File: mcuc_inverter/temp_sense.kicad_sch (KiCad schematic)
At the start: 0 parts

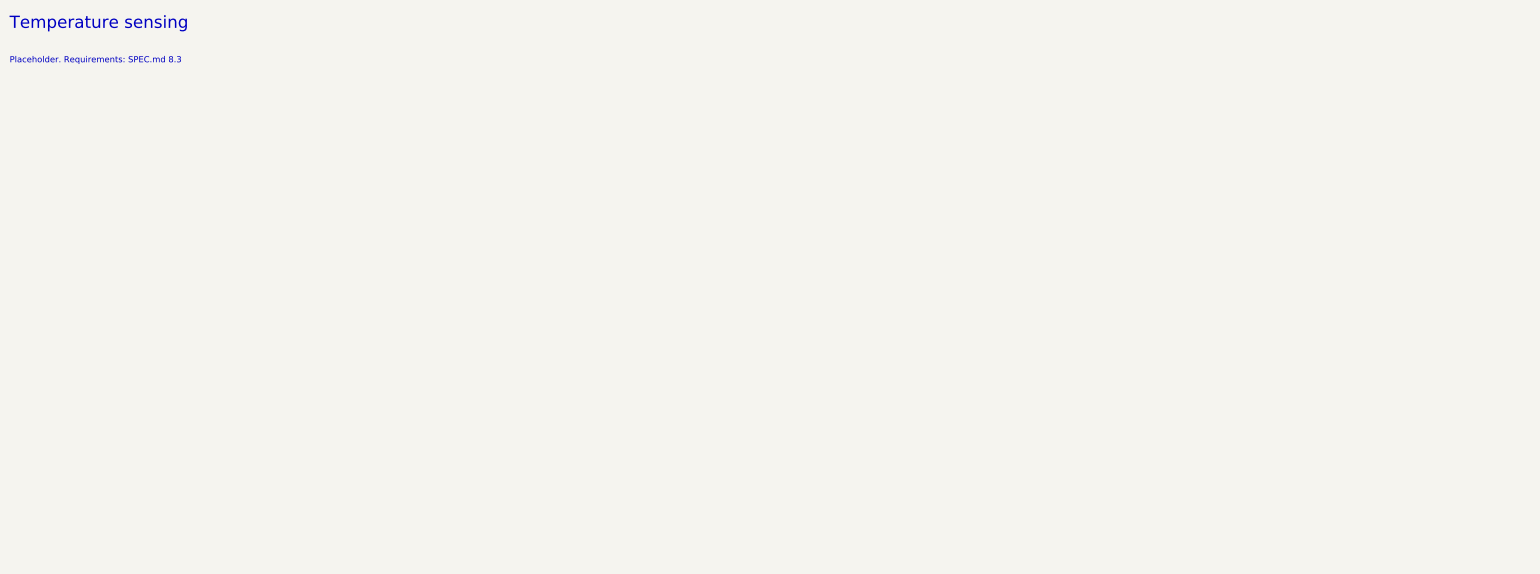
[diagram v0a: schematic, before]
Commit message: Capture bus_sense, temp_sense, comms: all 11 sheets now live
bus_sense: 4x750k + 12.0k string (strict series, 124.5 V/part) into
AMC1311BDWV (pinout verified vs SBAS786C; B-grade 3.0-5.5 V VDD1 is
load-bearing per D022; no input clamp diodes per TI 9.3), HV-side
3.3 V from MCP1804T-3302 (2-28 V in, stocked - no TBV needed) off
the VGD_LS rail, diff-to-SE gain 0.75: V_BUS = 2.988 mV/V, 500 V ->
1.494 V, saturates ~1.50 V, always < 3.3 V.

temp_sense: coldplate NTC channel (B57861S off-board via J1101),
board NTC (NCU18 successor), 6x DNP TS provision pads onto the
module TS pins with D022 rationale quoted on-sheet.

comms: ISO1042DWR isolated CAN (VCC2 pins 11/16 tied - datasheet
requirement), split termination + TVS added (legacy sheet flagged
its own missing protection), USB-C + USBLC6 to MCU 70/71, keyed SWD,
status LEDs, I/O connectors. CAN_TX/RX verified onto MCU pins 96/95;
CONTACTOR_P/N resolve onto the precharge coil driver.

ERC 0 errors; netlist machine-checks per sheet; key cross-sheet
nets independently re-verified. 11 of 11 sheets captured.

Co-Authored-By: Claude Fable 5 <noreply@anthropic.com>
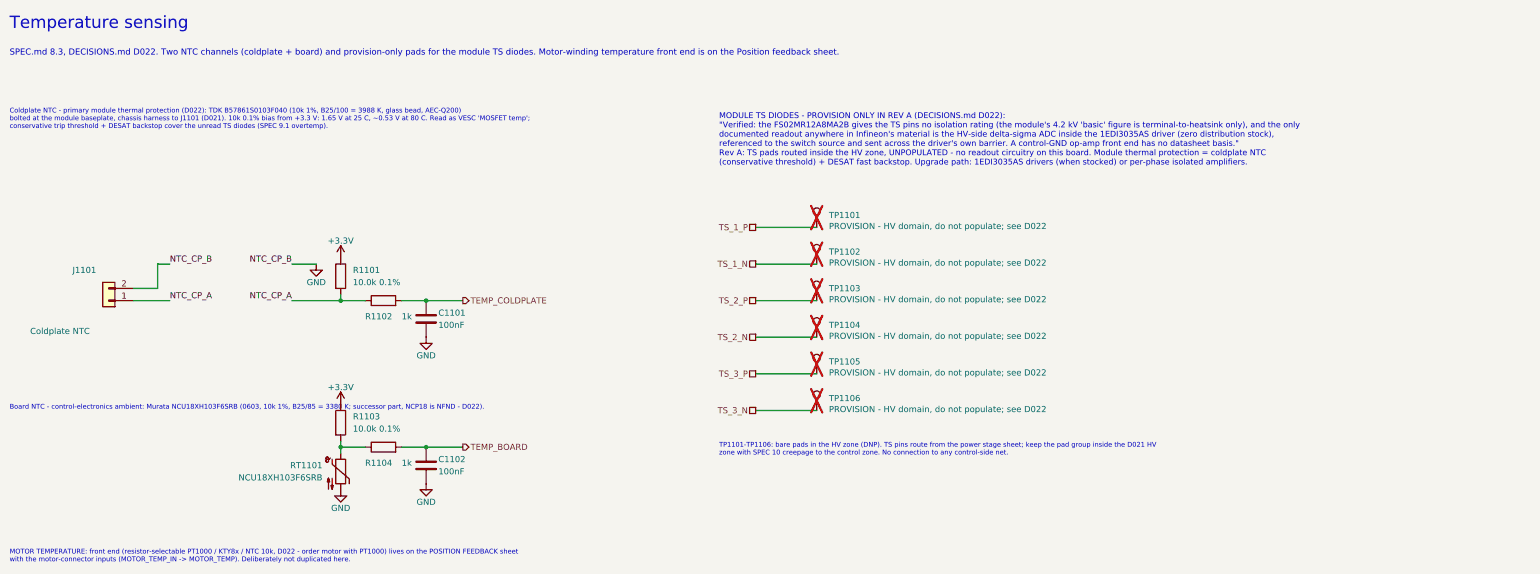
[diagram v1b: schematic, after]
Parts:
- added C1101, C1102: 100nF, Capacitor_SMD:C_0603_1608Metric, symbol Device:C
- added J1101: Coldplate NTC, Connector_JST:JST_PH_B2B-PH-K_1x02_P2.00mm_Vertical, symbol Connector_Generic:Conn_01x02
- added R1101, R1103: 10.0k 0.1%, Resistor_SMD:R_0603_1608Metric, symbol Device:R
- added R1102, R1104: 1k, Resistor_SMD:R_0603_1608Metric, symbol Device:R
- added RT1101: NCU18XH103F6SRB, Resistor_SMD:R_0603_1608Metric, symbol Device:Thermistor_NTC
- added TP1101, TP1102, TP1103, TP1104, TP1105, TP1106: PROVISION - HV domain, do not populate; see D022, TestPoint:TestPoint_Pad_D1.5mm, symbol Connector:TestPoint
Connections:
- new net: R1103.2, R1104.1, RT1101.1
- new net +3.3V: R1101.1, R1103.1
- new net GND: C1101.2, C1102.2, J1101.2 (Pin_2), RT1101.2
- new net NTC_CP_A: J1101.1 (Pin_1), R1101.2, R1102.1
- new net TEMP_BOARD: C1102.1, R1104.2
- new net TEMP_COLDPLATE: C1101.1, R1102.2
- new net TS_1_N: TP1102.1
- new net TS_1_P: TP1101.1
- new net TS_2_N: TP1104.1
- new net TS_2_P: TP1103.1
- new net TS_3_N: TP1106.1
- new net TS_3_P: TP1105.1
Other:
- note added: "Board NTC - control-electronics ambient: Murata NCU18XH103F6SRB (0603, 10k 1%, B25/85 = 3380 K; successor part, NCP18 is NFND - D022)."
- note added: "Coldplate NTC - primary module thermal protection (D022): TDK B57861S0103F040 (10k 1%, B25/100 = 3988 K, glass bead, AEC-Q200) bolted at the module baseplate, chassis harness to J1101 (D021). 10k 0.1% bias from +3.3 V: 1.65 V at 25 C, ~0.53 V at 80 C. Read as VESC 'MOSFET temp'; conservative trip threshold + DESAT backstop cover the unread TS diodes (SPEC 9.1 overtemp)."
- note added: "MODULE TS DIODES - PROVISION ONLY IN REV A (DECISIONS.md D022): "Verified: the FS02MR12A8MA2B gives the TS pins no isolation rating (the module's 4.2 kV 'basic' figure is terminal-to-heatsink only), and the only documented readout anywhere in Infineon's material is the HV-side delta-sigma ADC inside the 1EDI3035AS driver (zero distribution stock), referenced to the switch source and sent across t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"
- note added: "MOTOR TEMPERATURE: front end (resistor-selectable PT1000 / KTY8x / NTC 10k, D022 - order motor with PT1000) lives on the POSITION FEEDBACK sheet with the motor-connector inputs (MOTOR_TEMP_IN -> MOTOR_TEMP). Deliberately not duplicated here."
- note added: "SPEC.md 8.3, DECISIONS.md D022. Two NTC channels (coldplate + board) and provision-only pads for the module TS diodes. Motor-winding temperature front end is on the Position feedback sheet."
- note added: "TP1101-TP1106: bare pads in the HV zone (DNP). TS pins route from the power stage sheet; keep the pad group inside the D021 HV zone with SPEC 10 creepage to the control zone. No connection to any control-side net."
- note removed: "Placeholder. Requirements: SPEC.md 8.3"
